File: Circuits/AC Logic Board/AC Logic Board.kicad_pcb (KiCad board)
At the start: 2 copper layers, 76.2 x 26.9 mm, 7 parts, among them J1 Input, J2 Output

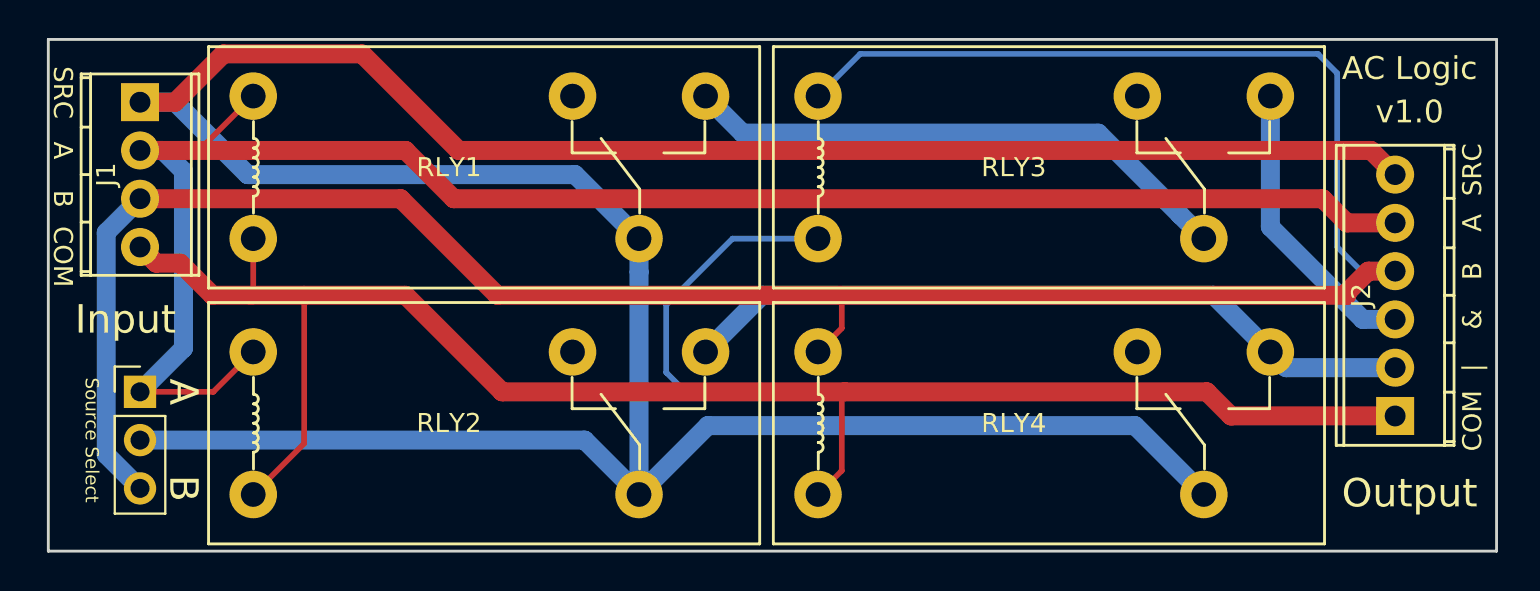
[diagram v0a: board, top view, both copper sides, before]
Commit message: AC Logic Board: differentiating AC Logic Board and a Pro version
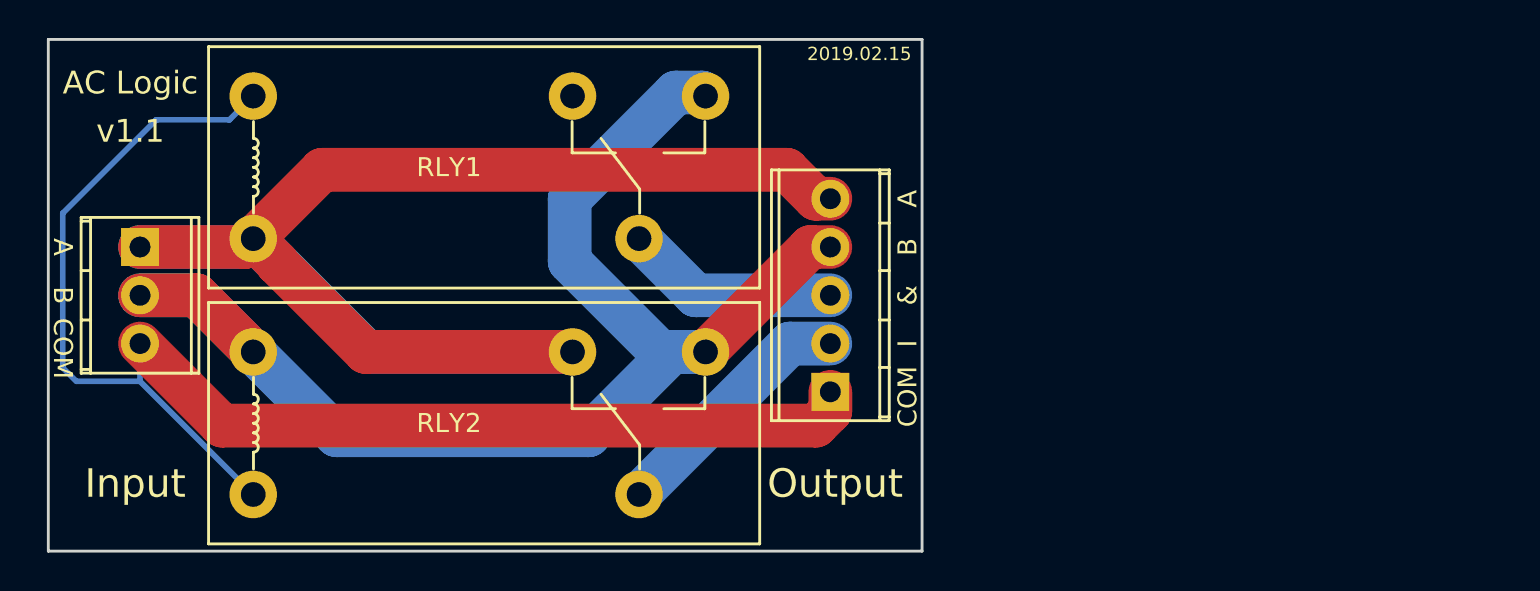
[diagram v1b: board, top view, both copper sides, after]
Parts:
- removed JP1: Source Select, Pin_Headers:Pin_Header_Straight_1x03_Pitch2.54mm
- removed RLY3: AND_B, Footprints:TE-RT1-3.5mm
- removed RLY4: OR_B, Footprints:TE-RT1-3.5mm
- J1: footprint TerminalBlocks_Phoenix:TerminalBlock_Phoenix_MPT-2.54mm_4pol -> Footprints:TerminalBlock_Phoenix_MPT-2.54mm_3pol
- J2: footprint TerminalBlocks_Phoenix:TerminalBlock_Phoenix_MPT-2.54mm_6pol -> TerminalBlocks_Phoenix:TerminalBlock_Phoenix_MPT-2.54mm_5pol
- RLY1: value AND_A -> A
- RLY2: value OR_A -> B
- moved J2 29.7 mm to (155.7, 94.0)
- moved J1 7.62 mm to (119.4, 86.4)
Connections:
- J1 pad 1: SOURCE -> A
- J1 pad 2: A -> B
- J1 pad 3: B -> COMMON
- RLY1 pad 11: SOURCE -> AND
- RLY1 pad 14: INT_AND -> B
- RLY1 pad A1: A -> COMMON
- RLY1 pad A2: COMMON -> A
- RLY2 pad 11: SOURCE -> OR
- RLY2 pad 12: Net-(RLY2-Pad12) -> A
- RLY2 pad 14: OR -> B
- RLY2 pad A1: A -> B
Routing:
- net SOURCE: track 172.6 -> 0.00 mm
- net COMMON: track 141.3 -> 74.9 mm
- net B: track 130.4 -> 72.6 mm
- net INT_AND: track 29.3 -> 0.00 mm
- net OR: track 39.1 -> 13.4 mm
- net A: track 96.9 -> 83.3 mm
- net AND: track 15.5 -> 11.3 mm
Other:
- board size 76.2 x 26.9 mm -> 46 x 26.9 mm
- net class High Current: trace_width 1 -> 2.3
- board text added: "2019.02.15"
- board text added: "I"
- board text added: "RLY1 (A)"
- board text added: "RLY2 (B)"
- board text added: "v1.1"
- board text removed: "I&"
- board text removed: "RLY1 (AND A)"
- board text removed: "RLY2 (OR A)"
- board text removed: "RLY3 (AND B)"
- board text removed: "RLY4 (OR B)"
- board text removed: "SRC"
- board text removed: "Source Select"
- board text removed: "v1.0"
- board text removed: "|"
